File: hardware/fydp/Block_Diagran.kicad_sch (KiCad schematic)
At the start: 0 parts

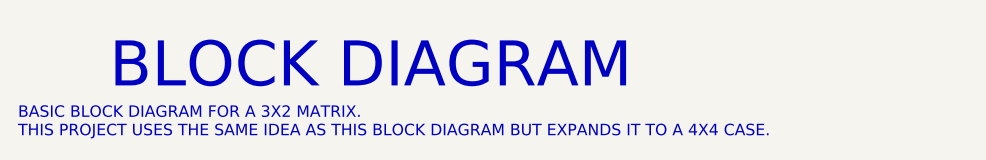
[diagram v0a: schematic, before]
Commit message: Edit schematic titles
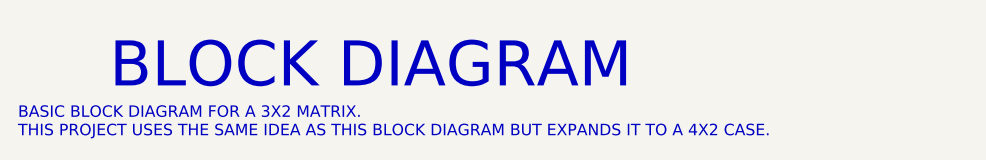
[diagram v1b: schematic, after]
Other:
- note added: "BASIC BLOCK DIAGRAM FOR A 3X2 MATRIX. THIS PROJECT USES THE SAME IDEA AS THIS BLOCK DIAGRAM BUT EXPANDS IT TO A 4X2 CASE."
- note removed: "BASIC BLOCK DIAGRAM FOR A 3X2 MATRIX. THIS PROJECT USES THE SAME IDEA AS THIS BLOCK DIAGRAM BUT EXPANDS IT TO A 4X4 CASE."
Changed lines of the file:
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@@
     (effects (font (size 5 5)) (justify left bottom))
   )
-  (text "BASIC BLOCK DIAGRAM FOR A 3X2 MATRIX.\nTHIS PROJECT USES THE SAME IDEA AS THIS BLOCK DIAGRAM BUT EXPANDS IT TO A 4X4 CASE."
+  (text "BASIC BLOCK DIAGRAM FOR A 3X2 MATRIX.\nTHIS PROJECT USES THE SAME IDEA AS THIS BLOCK DIAGRAM BUT EXPANDS IT TO A 4X2 CASE."
     (at 105.41 29.21 0)
     (effects (font (size 1.27 1.27)) (justify left bottom))
